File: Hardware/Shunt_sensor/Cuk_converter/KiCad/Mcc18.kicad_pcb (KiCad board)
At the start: 2 copper layers, 94 parts, among them Q1 IRFP4321PbF, U1 INA240, U2 DRIVER_(INEP), U3 LM7812_TO220, U4 Signals_MCC, U5 ZCS

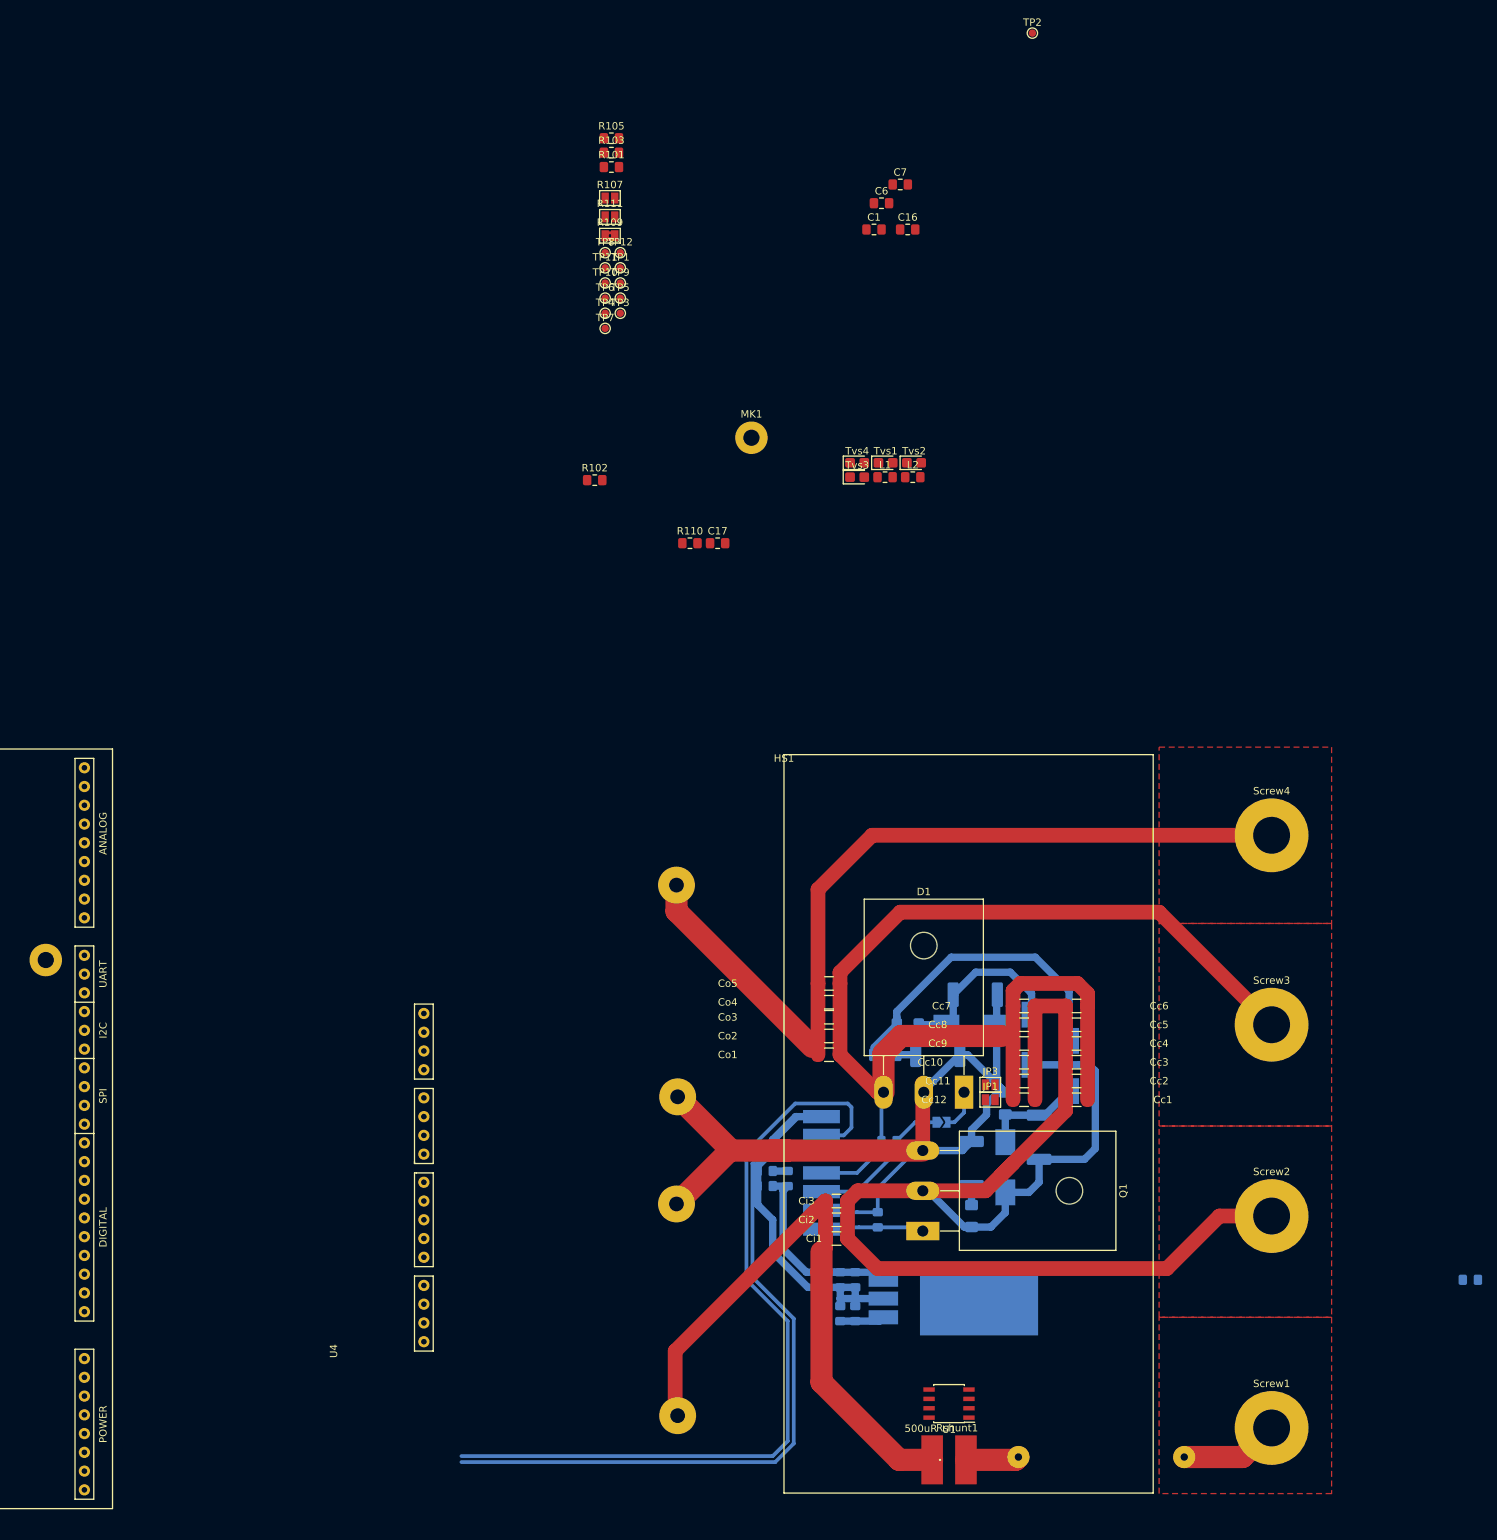
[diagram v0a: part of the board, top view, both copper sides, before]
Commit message: Finlized signals basic routing
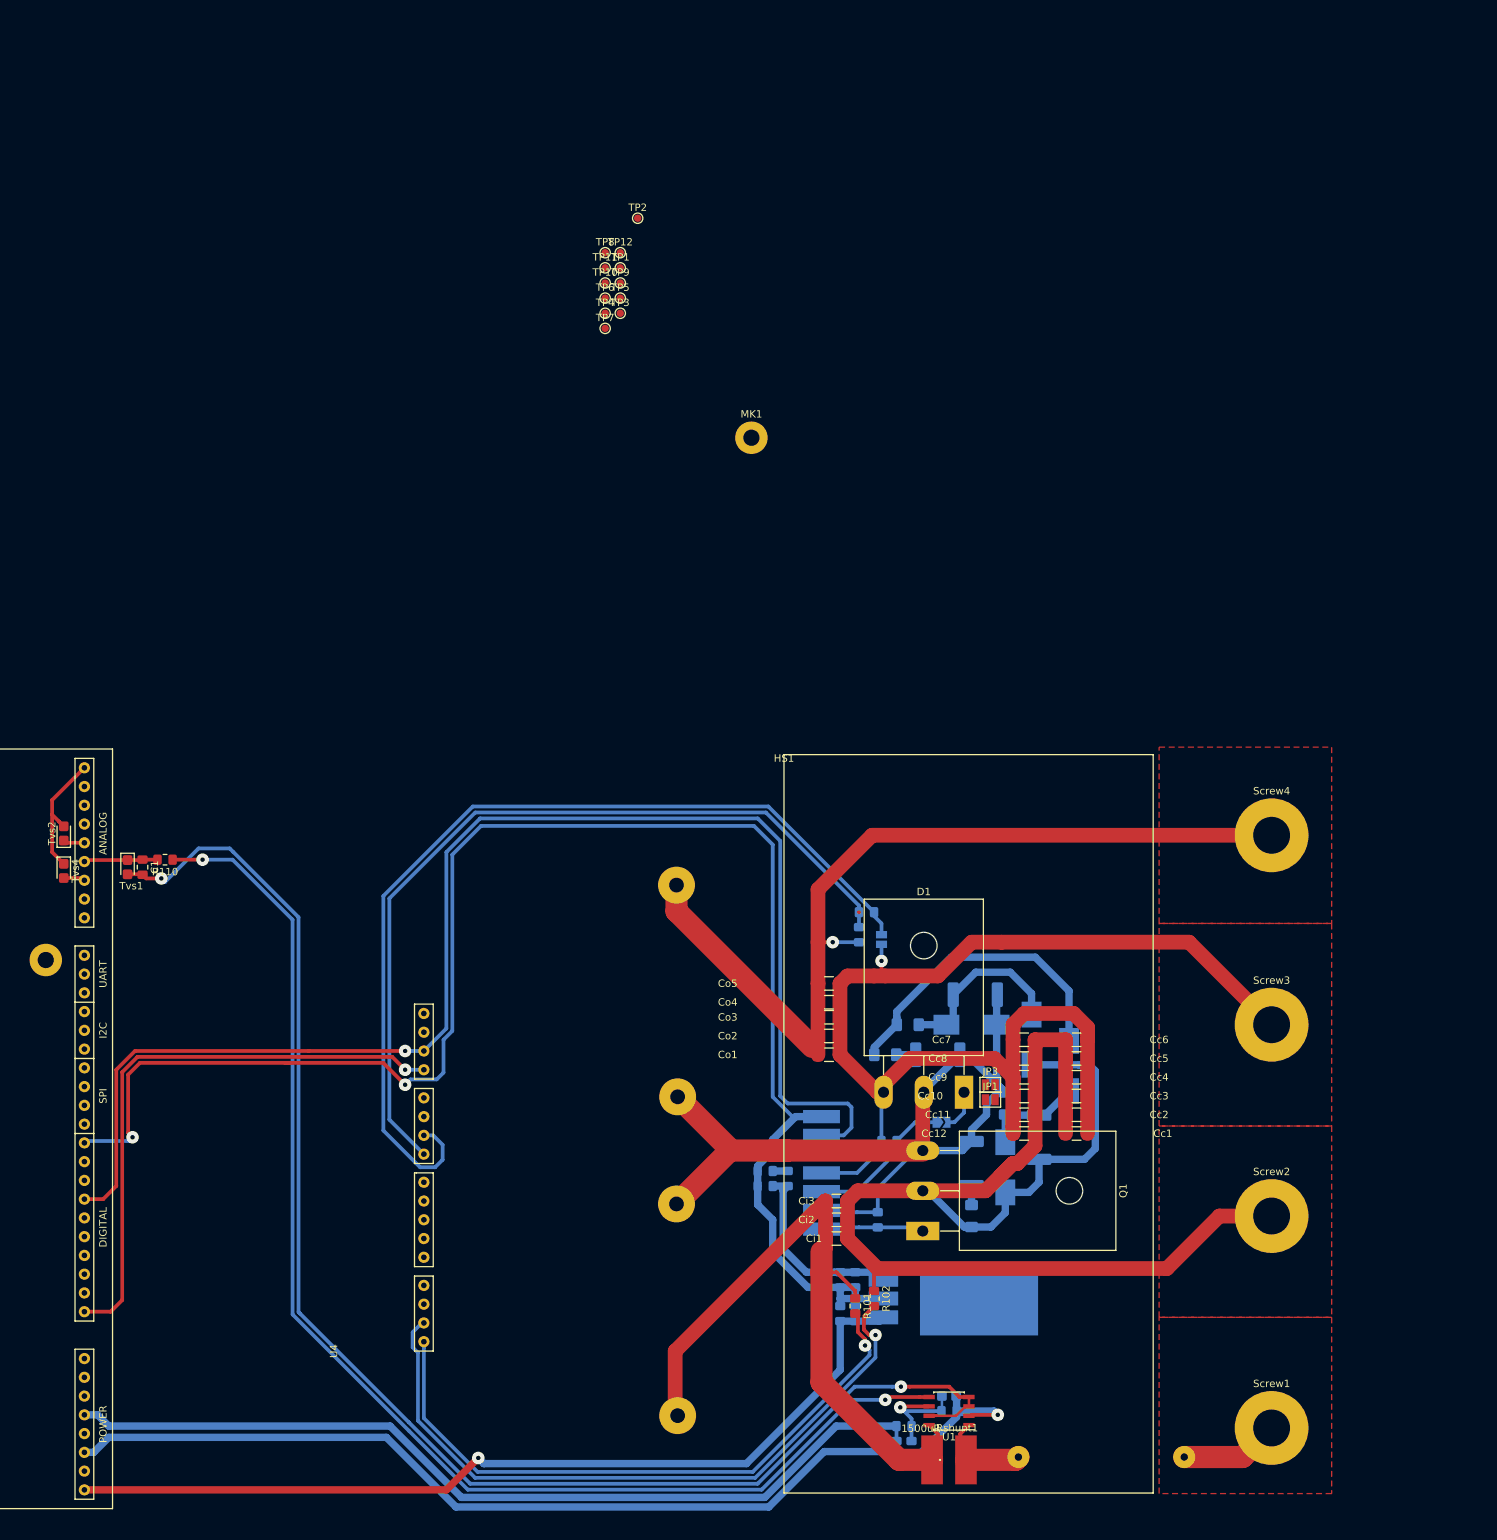
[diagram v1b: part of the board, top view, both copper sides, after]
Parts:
- removed C6, C7: 100nF, Capacitor_SMD:C_0805_2012Metric_Pad1.15x1.40mm_HandSolder
- removed L2: L_Small, Inductor_SMD:L_0805_2012Metric_Pad1.15x1.40mm_HandSolder
- removed R107, R111: 0R, Jumper:SolderJumper-2_P1.3mm_Open_Pad1.0x1.5mm
- removed R109: ??, Jumper:SolderJumper-2_P1.3mm_Bridged2Bar_Pad1.0x1.5mm
- added JP4: VBat-Sen, Jumper:SolderJumper-2_P1.3mm_Open_Pad1.0x1.5mm, B.Cu at (188.5, 69.2)
- C1: value 100nF -> 1uF
- C16, C17, L1, R103, R105, Tvs3: moved to B.Cu
- R110: value ?? -> 100
- Rshunt1: value 500uR -> 1500uR
- moved C16 165.1 mm to (192.5, 138.2), turned to 270 degrees
- moved R101 157.7 mm to (184.9, 118.9), turned to 270 degrees
- moved C1 131.4 mm to (88.4, 59.4), turned to 270 degrees
- moved L1 128.5 mm to (191.5, 135.1), turned to 180 degrees
- moved Tvs2 125.6 mm to (77.7, 54.9), turned to 90 degrees
- moved Tvs3 125.1 mm to (197.6, 131.1)
- moved C17 125.0 mm to (190.5, 138.2), turned to 270 degrees
- moved Tvs4 120.8 mm to (77.7, 59.9), turned to 270 degrees
- moved R102 117.1 mm to (187.5, 117.9), turned to 270 degrees
- moved Tvs1 116.4 mm to (86.4, 59.4), turned to 270 degrees
- moved R103 111.1 mm to (185.4, 68.6), turned to 90 degrees
- moved R105 110.4 mm to (186.4, 65.5), turned to 180 degrees
- moved R110 83.0 mm to (91.4, 58.4), turned to 180 degrees
- moved C11 72.8 mm to (197.6, 133.1), turned to 180 degrees
- moved TP2 59.0 mm to (155.4, -28.4)
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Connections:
- C11 pad 1: GNDA -> GND
- C16 pad 2: GNDA -> GND
- C17 pad 2: GNDA -> GND
- R105 pad 1: /-B -> /Vb_sen-
- R110 pad 1: /Ip_sen+ -> /INA240_OUT
- TP2 pad 1: /-B -> /Vb_sen-
- Tvs3 pad 2: GNDA -> GND
- U1 pad 2: GNDA -> GND
- U4 pad 11: /-B -> /Vb_sen-
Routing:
- net GND: track 147.5 -> 380.5 mm, vias 0 -> 3
- net GNDA: track 0.00 -> 215.3 mm, vias 0 -> 2
- net /INA240_OUT: track 0.00 -> 174.3 mm, vias 0 -> 2
- net /Vb_sen-: track 0.00 -> 128.2 mm
- net +5V: track 0.00 -> 120.6 mm
- net /+18V_OUT: track 6.06 -> 122.4 mm, vias 0 -> 1
- net /Vb_sen+: track 0.00 -> 113.1 mm
- net /Vp_sen+: track 0.00 -> 94.9 mm, vias 0 -> 1
- net /Vp_sen-: track 0.00 -> 86.7 mm, vias 0 -> 1
- net /PWM: track 110.9 -> 192.1 mm, vias 0 -> 1
- net /BatOVInterrupt: track 0.00 -> 79.1 mm, vias 0 -> 1
- net +5VA: track 0.00 -> 17.0 mm, vias 0 -> 1
- net /-Vp: track 82.1 -> 94.2 mm
- net /Ipanel_adc+: track 0.00 -> 10.0 mm
- net /-B: track 209.4 -> 216.8 mm, vias 0 -> 1
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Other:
- net class Default: clearance 0.3048 -> 0.295
- rule trace_clearance: 0.3048 -> 0.295
- rule trace_min: 0.0508 -> 0.0499

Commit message: Added ADC tracks
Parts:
- moved C1 12.7 mm to (101.1, 59.9)
- moved R110 12.7 mm to (104.1, 58.9)
- moved Tvs1 12.7 mm to (99.1, 59.9)
- moved Tvs2 12.7 mm to (90.4, 54.9)
- moved Tvs4 12.7 mm to (90.4, 59.9)
- moved U5 12.7 mm to (51.3, 146.3)
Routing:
- net GNDA: track 215.3 -> 376.3 mm, vias 2 -> 8
- net /Vpanel_adc+: track 2.92 -> 87.0 mm, vias 0 -> 2
- net GND: track 380.5 -> 461.1 mm, vias 3 -> 4
- net /Vbat_adc+: track 2.92 -> 68.9 mm, vias 0 -> 2
- net /BatOVInterrupt: track 79.1 -> 66.4 mm
- net /+18V_OUT: track 122.4 -> 109.7 mm
- net /PWM: track 192.1 -> 179.4 mm
- net +5V: track 120.6 -> 107.9 mm
- net /INA240_OUT: track 174.3 -> 168.4 mm
- net /Ipanel_adc+: track 10.0 -> 9.39 mm

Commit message: Some 3D added, power reworked to minimize stray inductances
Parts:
- L1/2, L2/2: moved to F.Cu
- moved JP4 223.6 mm to (411.1, 48.4)
- moved R103 223.6 mm to (408.1, 47.8)
- moved R105 223.6 mm to (409.1, 44.7)
- moved R101 222.9 mm to (407.8, 115.6)
- moved Tvs2 222.9 mm to (313.3, 51.6)
- moved Tvs4 222.9 mm to (313.3, 56.6)
- moved C1 222.9 mm to (324.0, 56.6)
- moved R102 222.9 mm to (410.3, 114.6)
- moved R110 222.9 mm to (327.0, 55.6)
- moved Tvs1 222.9 mm to (321.9, 56.6)
- moved U5 125.9 mm to (124.5, 43.8), turned to 270 degrees
- moved L1/2 52.6 mm to (129.5, 86.4), turned to 90 degrees
- moved U2 52.0 mm to (194.7, 64.8), turned to 180 degrees
- moved U4 40.8 mm to (127.0, 86.4), turned to 270 degrees
- moved Cc6 38.7 mm to (177.8, 94.0), turned to 90 degrees
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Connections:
- Cs12 pad 1: Net-(Cs12-Pad1) -> /HS
- Cs12 pad 2: /-B -> Net-(Cs12-Pad2)
- L1/2 pad 1: /+B -> /HS
- L1/2 pad 2: /HS -> /+B
- L2/2 pad 1: /HS -> /-Vp
- L2/2 pad 2: /-Vp -> /HS
- Rs2 pad 1: /HS -> Net-(Cs12-Pad2)
- Rs2 pad 2: Net-(Cs12-Pad1) -> /-B
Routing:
- net /+B: track 121.9 -> 425.0 mm
- net /-B: track 216.8 -> 472.2 mm, vias 1 -> 0
- net /+Vp: track 185.2 -> 419.1 mm
- net /-Vp: track 94.2 -> 291.2 mm
- net /HS: track 124.2 -> 210.7 mm, vias 0 -> 4
- net GND: track 461.1 -> 415.8 mm
- net Net-(D1-Pad1): track 5.51 -> 37.7 mm
- net /Vb_sen-: track 128.2 -> 108.0 mm
- net /Vb_sen+: track 113.1 -> 95.3 mm
- net /PWM: track 179.4 -> 161.9 mm
- net /LG: track 20.3 -> 3.92 mm
- net +12V: track 26.1 -> 11.2 mm
- net Net-(Cs14-Pad2): track 13.8 -> 21.0 mm
- net /+18V_OUT: track 109.7 -> 103.1 mm
- net Net-(Cs12-Pad2): track 0.00 -> 6.40 mm
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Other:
- board outline added: 177.8 x 104.1 mm

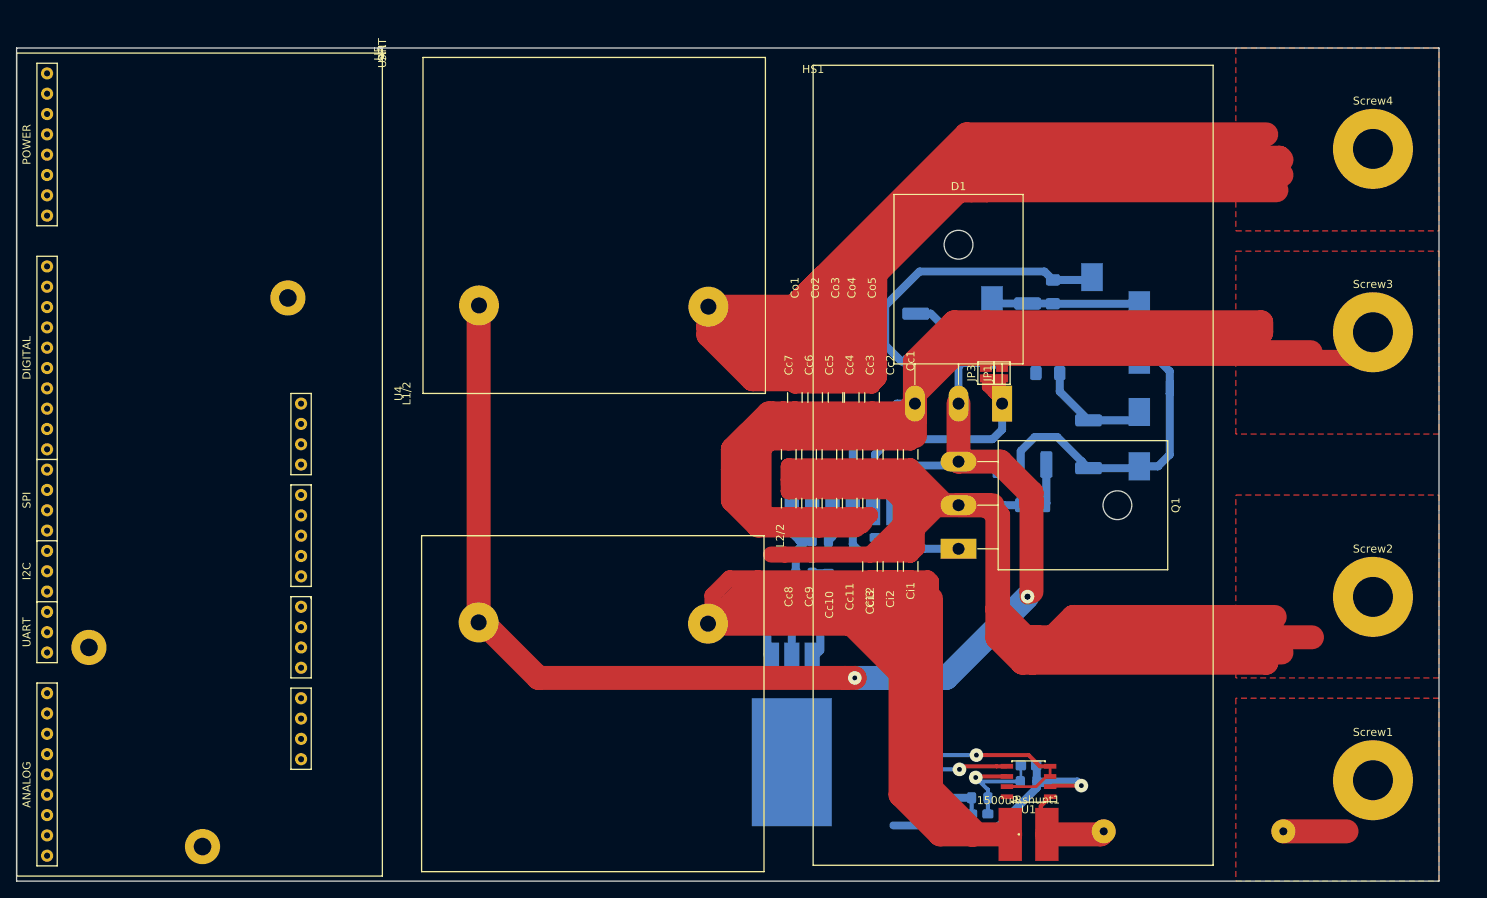
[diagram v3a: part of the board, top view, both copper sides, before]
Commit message: Added fill zones
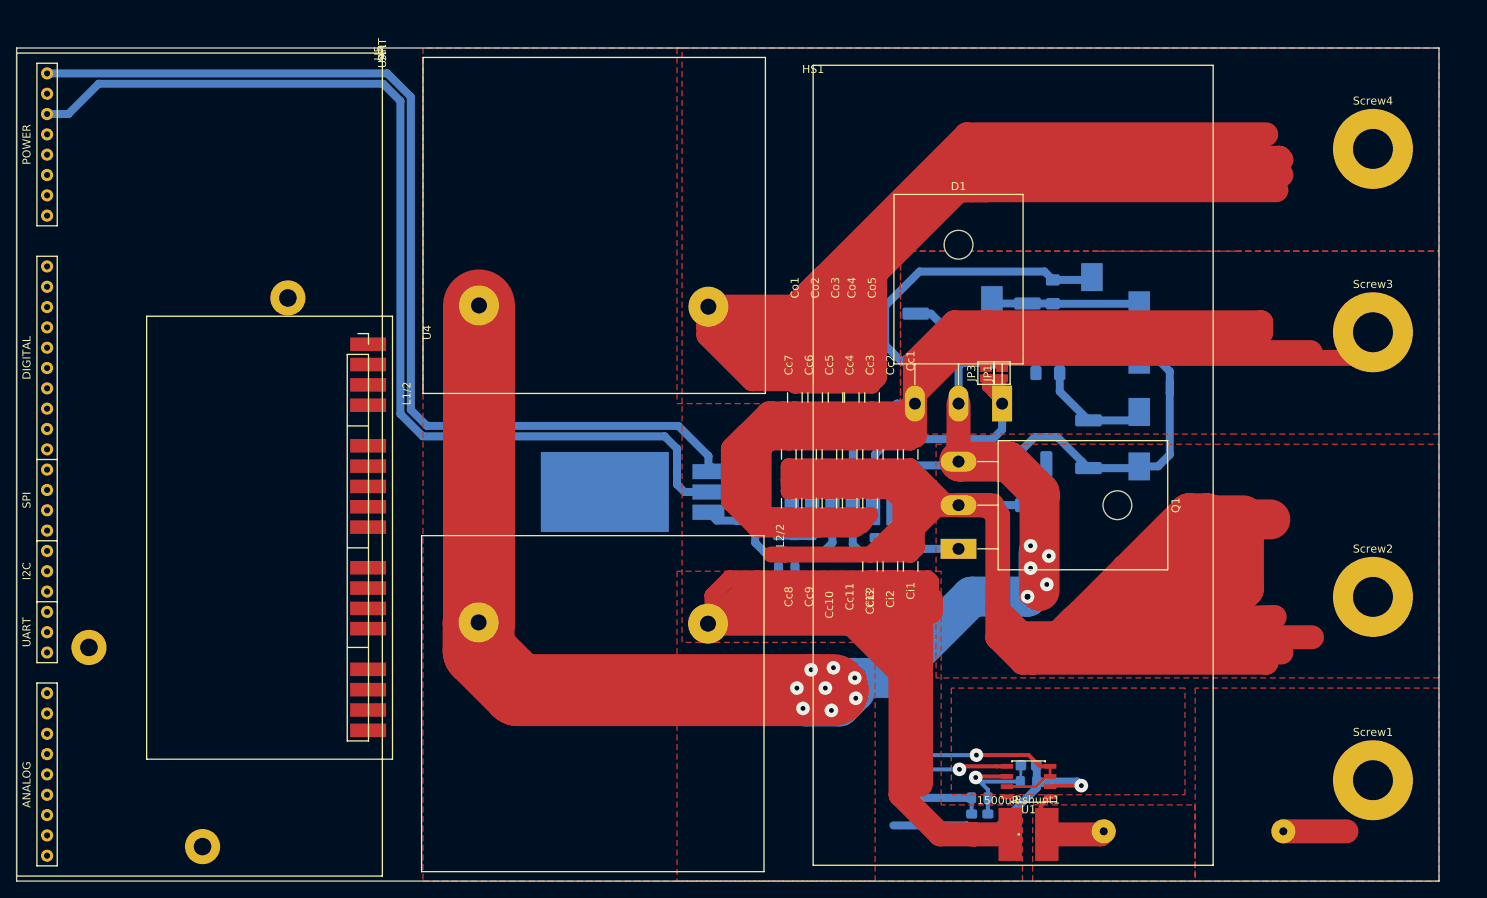
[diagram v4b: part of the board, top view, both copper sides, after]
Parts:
- U4: footprint MCCplaca:Signals -> MCCplaca:SignalsBarrapinos_SMD
- moved U3 26.3 mm to (164.0, 96.1), turned to 270 degrees
- moved C2 19.6 mm to (169.0, 96.6), turned to 270 degrees
- moved C3 17.2 mm to (171.1, 96.6), turned to 270 degrees
- moved C4 17.1 mm to (169.0, 101.2), turned to 90 degrees
- moved C5 14.3 mm to (171.1, 101.2), turned to 90 degrees
- moved U4 9.74 mm to (125.7, 76.7)
- moved L3 5.22 mm to (175.0, 108.2), turned to 0 degrees
- moved C8 4.86 mm to (174.0, 105.2), turned to 90 degrees
- moved C9 2.01 mm to (176.0, 105.2), turned to 90 degrees
- moved C10 1.20 mm to (178.1, 105.2), turned to 90 degrees
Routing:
- net GND: track 415.8 -> 551.4 mm
- net /+18V_OUT: track 103.1 -> 230.4 mm
- net /+Vp: track 419.1 -> 506.7 mm
- net /-Vp: track 291.2 -> 248.7 mm
- net /HS: track 210.7 -> 245.1 mm, vias 4 -> 15
- net +12V: track 11.2 -> 14.5 mm
- net Net-(C10-Pad1): track 8.71 -> 11.9 mm
- added copper zone on F.Cu, net /-Vp
- added copper zone on F.Cu, net /HS
- added copper zone on F.Cu, net /Rs-
- added copper zone on F.Cu, net GND
